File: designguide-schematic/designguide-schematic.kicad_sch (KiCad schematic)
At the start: 47 parts, among them J1 HRO_TYPE-C-31-M-14, J2 UDB, J3 Battery, J4 Battery, J5 Thermistor, Q1 AO3401A, Q2 2N7002, SW1 PWR, U1 SRV05-4, U2 TP4056, U3 BQ24075

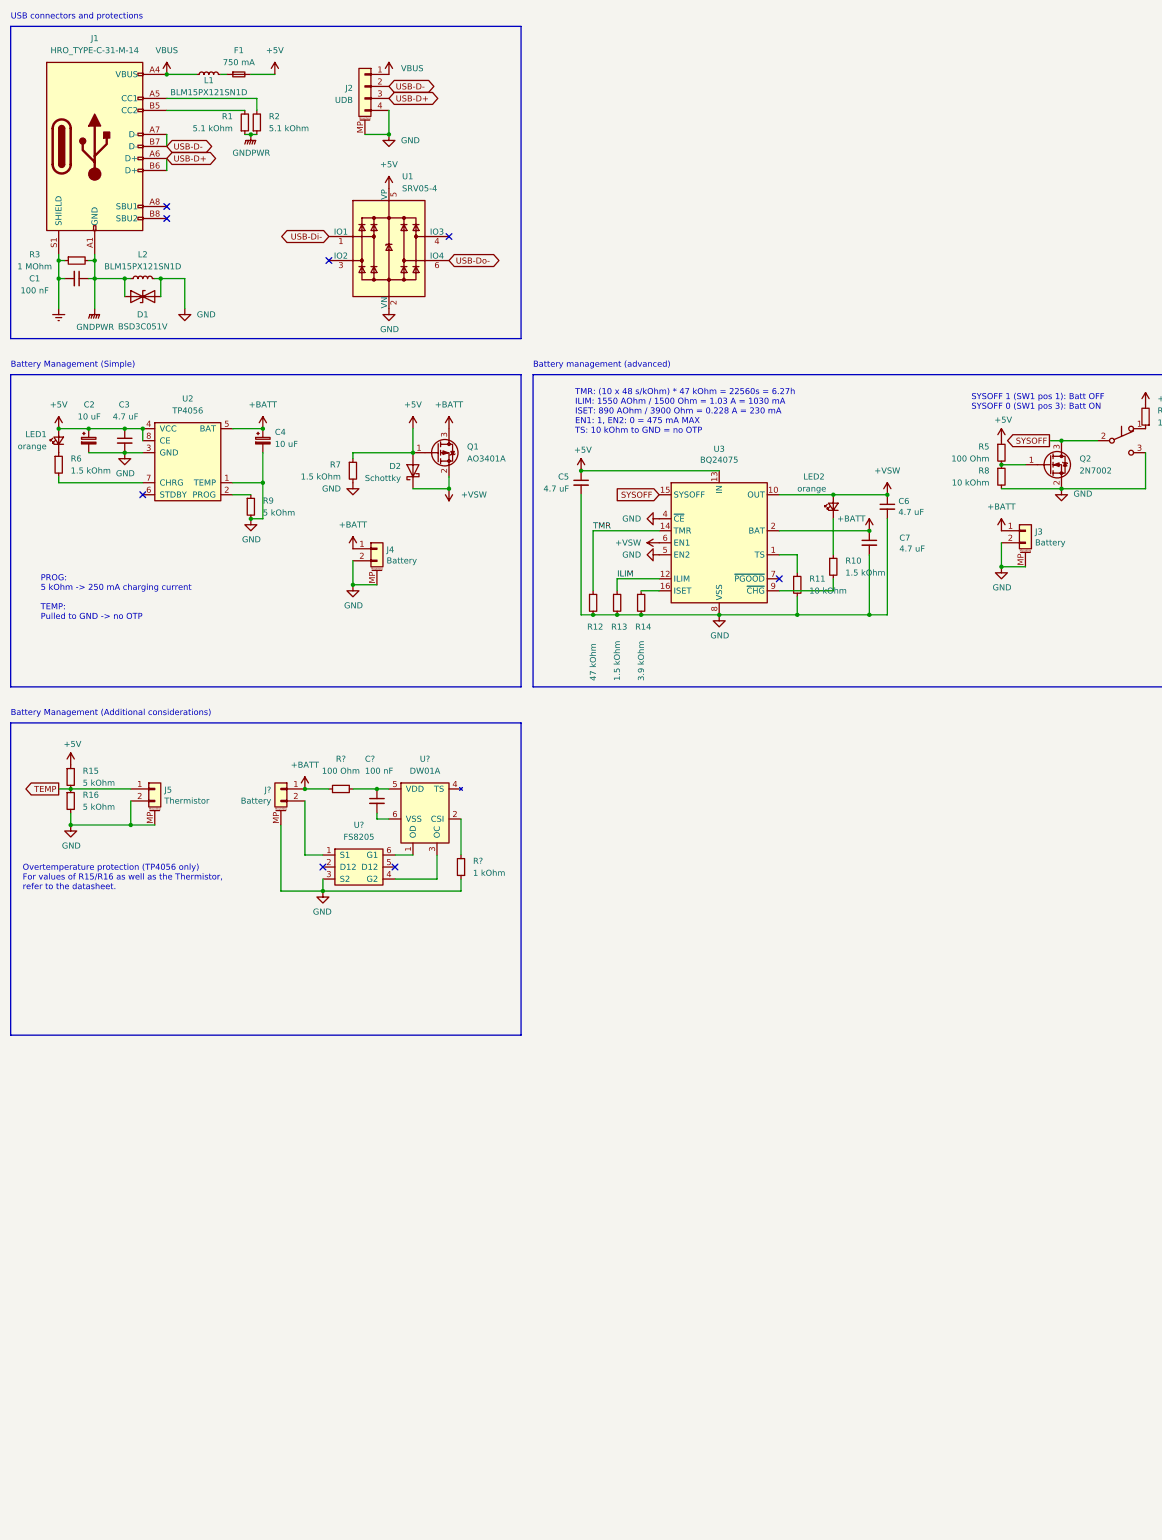
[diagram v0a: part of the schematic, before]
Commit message: readied battery management, usb, mcu parts
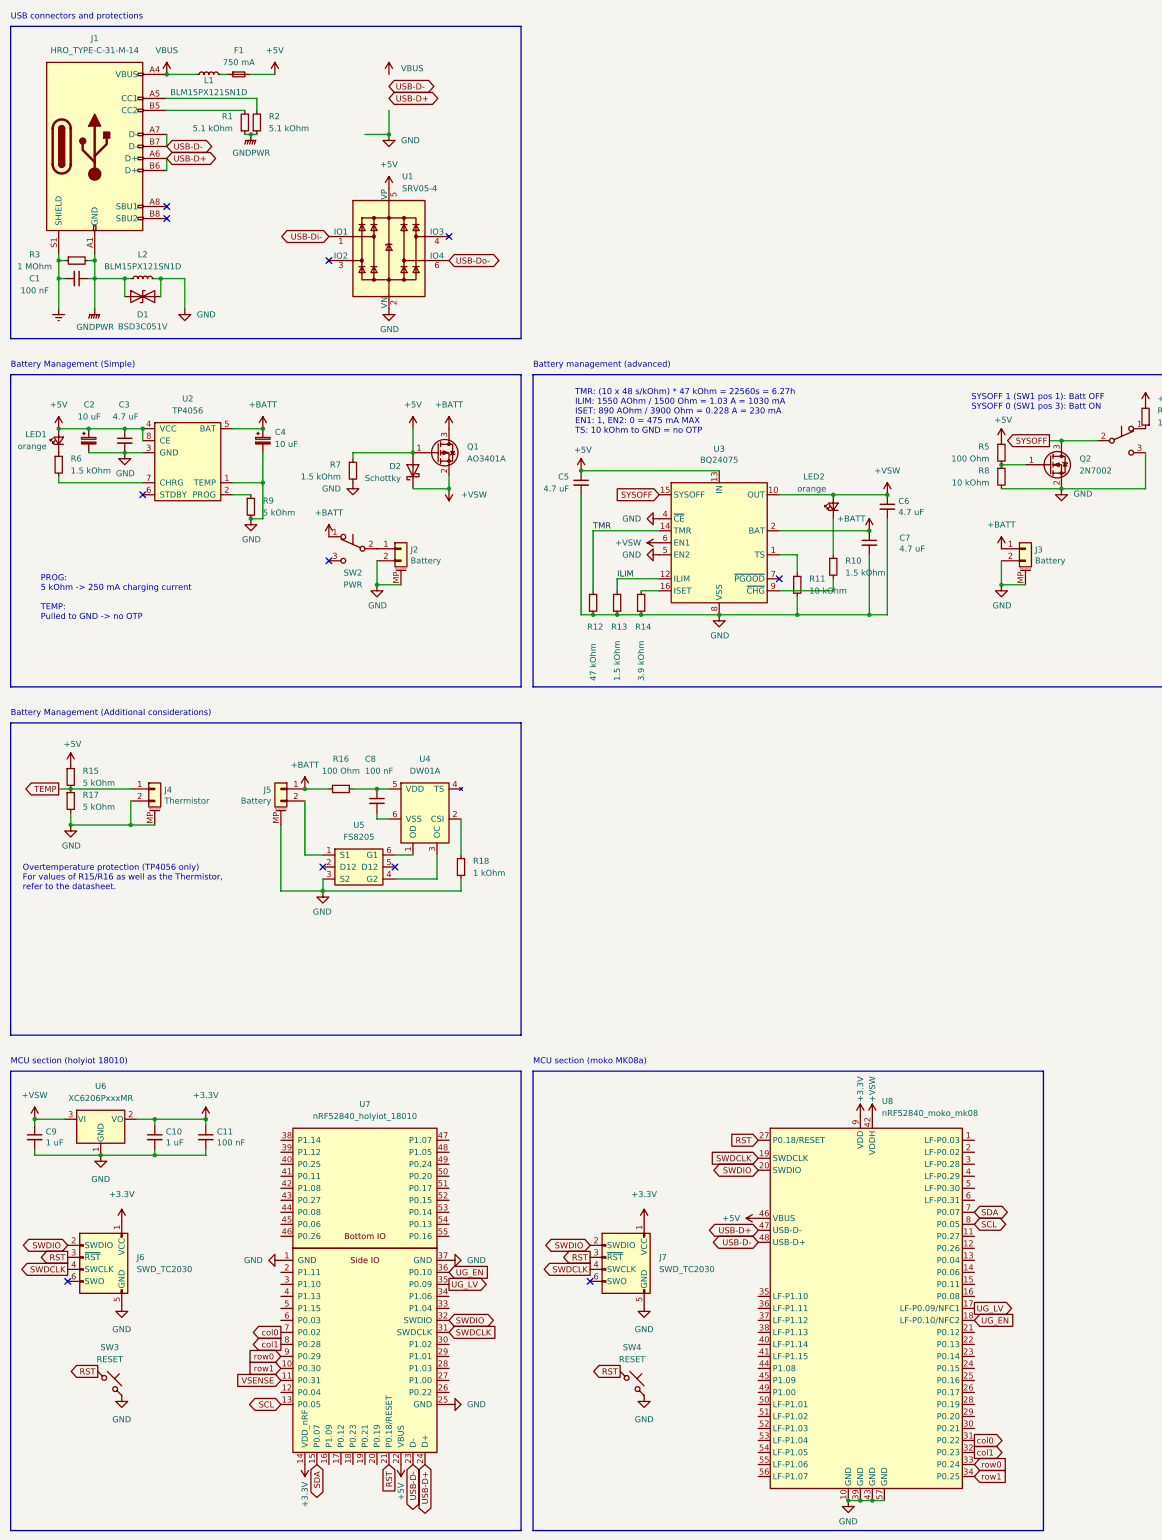
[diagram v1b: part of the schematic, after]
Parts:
- removed J2: UDB, Connector_JST:JST_SH_SM02B-SRSS-TB_1x02-1MP_P1.00mm_Horizontal, symbol Connector_Generic_MountingPin:Conn_01x04_MountingPin
- added C10, C9: 1 uF, Capacitor_SMD:C_0402_1005Metric, symbol Device:C_Small
- added C11: 100 nF, Capacitor_SMD:C_0402_1005Metric, symbol Device:C_Small
- added J6, J7: SWD_TC2030, marbastlib-various:CON_TC2030_outlined, symbol marbastlib-various:JTAG_TC2030
- added SW2: PWR, marbastlib-various:SW_MSK12C02-HB, symbol Switch:SW_Push_SPDT
- added SW3, SW4: RESET, symbol Switch:SW_Push_45deg
- added U6: XC6206PxxxMR, Package_TO_SOT_SMD:SOT-23, symbol Regulator_Linear:XC6206PxxxMR
- added U7: nRF52840_holyiot_18010, marbastlib-various:nRF52840_holyiot_18010, symbol marbastlib-various:nRF52840_holyiot_18010
- added U8: nRF52840_moko_mk08, marbastlib-various:nRF52840_moko_mk08, symbol marbastlib-various:nRF52840_moko_mk08
- gave numbers to parts that had none: 6
- renumbered J4 to J2, J5 to J4, R16 to R17
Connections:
- net +5V: now also U7.22 (VBUS), U8.46 (VBUS)
- net +BATT: now also SW2.1 (A); no longer J2.1 (Pin_1)
- net +VSW: now also C9.1, U6.3 (VI), U8.42 (VDDH)
- net GND: now also C10.2, C11.2, C9.2, J6.5 (GND), J7.5 (GND), SW3.2, SW4.2, U6.1 (GND), U7.1 (GND), U7.25 (GND), U7.37 (GND), U8.10 (GND), U8.39 (GND), U8.43 (GND), U8.57 (GND)
- net USB-D+: now also U7.24 (D+), U8.47 (USB-D-)
- net USB-D-: now also U7.23 (D-), U8.48 (USB-D+)
- new net: J2.1 (Pin_1), SW2.2 (B)
- new net +3.3V: C10.1, C11.1, J6.1 (VCC), J7.1 (VCC), U6.2 (VO), U7.14 (VDD_nRF), U8.9 (VDD)
- new net RST: J6.3 (~{RST}), J7.3 (~{RST}), SW3.1, SW4.1, U7.21 (P0.18/RESET), U8.27 (P0.18/RESET)
- new net SCL: U7.13 (P0.05), U8.8 (P0.05)
- new net SDA: U7.15 (P0.07), U8.7 (P0.07)
- new net SWDCLK: J6.4 (SWCLK), J7.4 (SWCLK), U7.31 (SWDCLK), U8.19 (SWDCLK)
- new net SWDIO: J6.2 (SWDIO), J7.2 (SWDIO), U7.32 (SWDIO), U8.20 (SWDIO)
- new net UG_EN: U7.36 (P0.10), U8.18 (LF-P0.10/NFC2)
- new net UG_LV: U7.35 (P0.09), U8.17 (LF-P0.09/NFC1)
- new net VSENSE: U7.11 (P0.31)
- new net col0: U7.7 (P0.02), U8.31 (P0.22)
- new net col1: U7.8 (P0.28), U8.32 (P0.23)
- new net row0: U7.9 (P0.29), U8.33 (P0.24)
- new net row1: U7.10 (P0.30), U8.34 (P0.25)
- no-connect marks 8 -> 11
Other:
- note added: "MCU section (holyiot 18010)"
- note added: "MCU section (moko MK08a)"
- moved on the sheet: J2, J3

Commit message: re-made images, finished schematic
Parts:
- added C12, C13, C14, C15, C16, C17, C18, C19: 100 nF, Capacitor_SMD:C_0402_1005Metric, symbol Device:C_Small
- added D3, D4, D5, D6: 1N4148WT, Diode_SMD:D_SOD-523, symbol Diode:1N4148WT
- added J2: UDB, symbol Connector_Generic_MountingPin:Conn_01x04_MountingPin
- added LED3, LED4, LED5, LED6, LED7, LED8, LED9: WS2812_2020, marbastlib-various:LED_WS2812_2020, symbol marbastlib-various:WS2812_2020
- added Q3: AO3401A, Package_TO_SOT_SMD:SOT-23, symbol Transistor_FET:AO3401A
- added Q4: 2N7002, Package_TO_SOT_SMD:SOT-23, symbol Transistor_FET:2N7002
- added R19, R20: 5.1 kOhm, Resistor_SMD:R_0402_1005Metric, symbol Device:R_Small
- added R21: 806 kOhm, Resistor_SMD:R_0402_1005Metric, symbol Device:R_Small
- added R22: 2 MOhm, Resistor_SMD:R_0402_1005Metric, symbol Device:R_Small
- added R23, R24, R26: 10 kOhm, Resistor_SMD:R_0402_1005Metric, symbol Device:R_Small
- added R25: 100 Ohm, Resistor_SMD:R_0402_1005Metric, symbol Device:R_Small
- added SW5, SW6, SW7, SW8: Keyswitch, symbol Switch:SW_Push_45deg
- added U10: TXB0101, Package_TO_SOT_SMD:SOT-363_SC-70-6_Handsoldering, symbol marbastlib-various:TXB0101
- added U9: MAX17048, Package_DFN_QFN:DFN-8-1EP_2x2mm_P0.5mm_EP0.7x1.3mm, symbol marbastlib-various:MAX17048
- renumbered J2 to J3, J3 to J4, J4 to J5, J5 to J6, J6 to J7, J7 to J8
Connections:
- net +3.3V: now also R19.2, R20.2, R23.1, U10.1 (VCCA)
- net +BATT: now also C12.2, U9.2 (CELL), U9.3 (VDD)
- net +VSW: now also Q3.3 (D), R21.1, R24.1, U10.6 (VCCB)
- net GND: now also C12.1, C13.1, C14.1, C15.1, C16.1, C17.1, C18.1, C19.1, J2.4 (Pin_4), J2.MP (MountPin), LED3.2 (VSS), LED4.2 (VSS), LED5.2 (VSS), LED6.2 (VSS), LED7.2 (VSS), LED8.2 (VSS), LED9.2 (VSS), Q4.2 (S), R22.2, R26.2, U10.2 (GND), U9.1 (CTG), U9.4 (GND), U9.6 (QSTRT), U9.9 (GND)
- net SCL: now also R19.1, U9.7 (SCL)
- net SDA: now also R20.1, U9.8 (SDA)
- net UG_EN: now also R25.1
- net UG_LV: now also U10.3 (A)
- net USB-D+: now also J2.3 (Pin_3)
- net USB-D-: now also J2.2 (Pin_2)
- net VBUS: now also J2.1 (Pin_1)
- net VSENSE: now also R21.2, R22.1
- net col0: now also SW5.1, SW7.1
- net col1: now also SW6.1, SW8.1
- net row0: now also D3.1 (K), D4.1 (K)
- net row1: now also D5.1 (K), D6.1 (K)
- new net: LED4.1 (DOUT), LED5.3 (DIN)
- new net: LED3.1 (DOUT), LED4.3 (DIN)
- new net: LED7.1 (DOUT), LED8.3 (DIN)
- new net: LED6.1 (DOUT), LED7.3 (DIN)
- new net: Q4.1 (G), R25.2, R26.1
- new net: Q3.1 (G), Q4.3 (D), R24.2
- new net: D3.2 (A), SW5.2
- new net: D5.2 (A), SW7.2
- new net: LED8.1 (DOUT), LED9.3 (DIN)
- new net: D6.2 (A), SW8.2
- new net: LED5.1 (DOUT), LED6.3 (DIN)
- new net: R23.2, U10.5 (OE)
- new net: D4.2 (A), SW6.2
- new net ALERT: U9.5 (~{ALRT})
- new net UG_HS: LED3.3 (DIN), U10.4 (B)
- new net UG_PWR: C13.2, C14.2, C15.2, C16.2, C17.2, C18.2, C19.2, LED3.4 (VDD), LED4.4 (VDD), LED5.4 (VDD), LED6.4 (VDD), LED7.4 (VDD), LED8.4 (VDD), LED9.4 (VDD), Q3.2 (S)
- no-connect marks 11 -> 12
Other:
- note added: "Switch matrix"
- note added: "Underglow enable"
- note added: "Underglow levelshifter"
- note added: "Voltage sensing (advanced)"
- note added: "Voltage sensing (simple) - Holyiot only!"

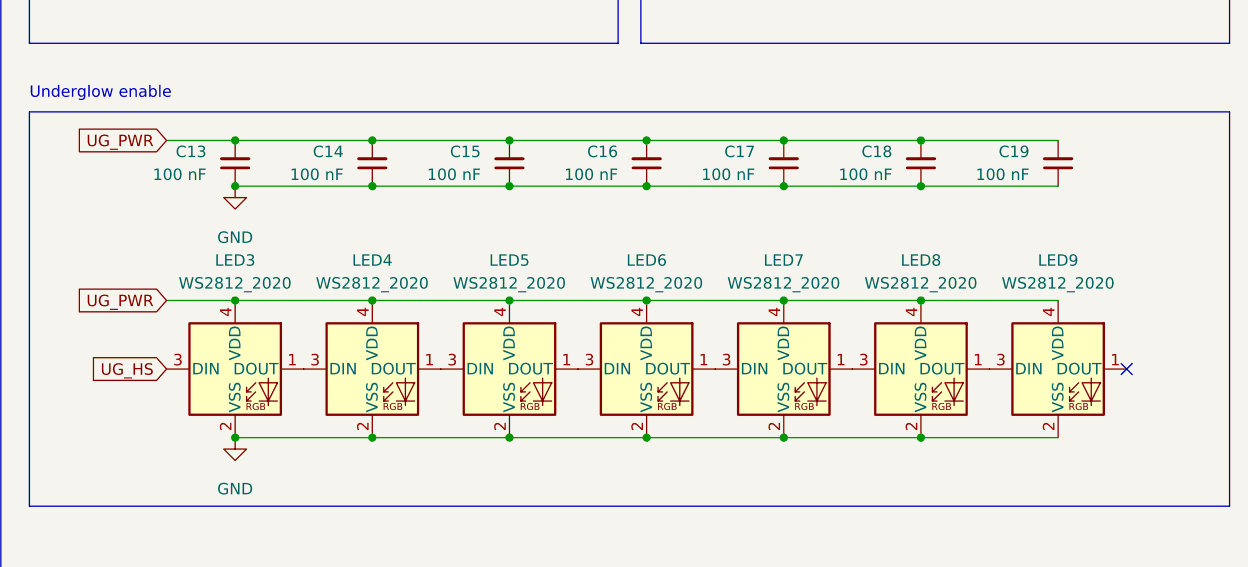
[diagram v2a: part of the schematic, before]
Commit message: included all pictures in the doc, changed underglow led model
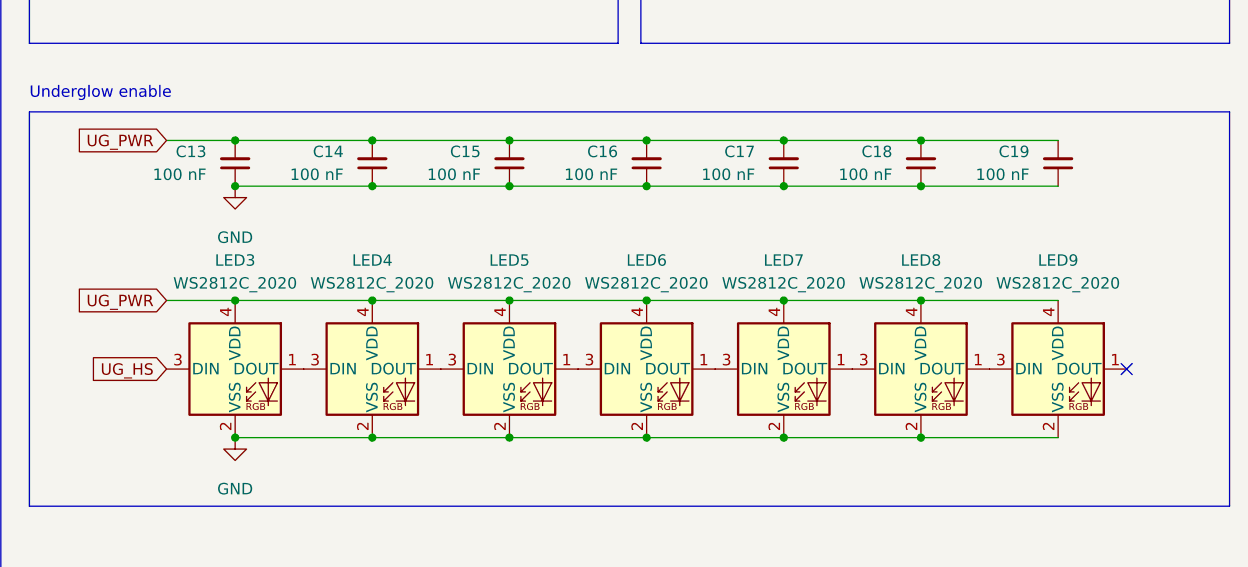
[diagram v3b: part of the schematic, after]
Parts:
- LED3, LED4, LED5, LED6, LED7, LED8, LED9: value WS2812_2020 -> WS2812C_2020
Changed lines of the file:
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@@
     (in_bom yes) (on_board yes)
     (property "Reference" "LED4" (id 0) (at 320.04 188.595 0))
-    (property "Value" "WS2812_2020" (id 1) (at 320.04 191.135 0))
+    (property "Value" "WS2812C_2020" (id 1) (at 320.04 191.135 0))
     (property "Footprint" "marbastlib-various:LED_WS2812_2020" (id 2) (at 321.31 208.28 0)
       (effects (font (size 1.27 1.27)) (justify left top) hide)
@@
     (in_bom yes) (on_board yes)
     (property "Reference" "LED7" (id 0) (at 365.76 188.595 0))
-    (property "Value" "WS2812_2020" (id 1) (at 365.76 191.135 0))
+    (property "Value" "WS2812C_2020" (id 1) (at 365.76 191.135 0))
     (property "Footprint" "marbastlib-various:LED_WS2812_2020" (id 2) (at 367.03 208.28 0)
       (effects (font (size 1.27 1.27)) (justify left top) hide)
@@
     (in_bom yes) (on_board yes)
     (property "Reference" "LED9" (id 0) (at 396.24 188.595 0))
-    (property "Value" "WS2812_2020" (id 1) (at 396.24 191.135 0))
+    (property "Value" "WS2812C_2020" (id 1) (at 396.24 191.135 0))
     (property "Footprint" "marbastlib-various:LED_WS2812_2020" (id 2) (at 397.51 208.28 0)
       (effects (font (size 1.27 1.27)) (justify left top) hide)
@@
     (in_bom yes) (on_board yes)
     (property "Reference" "LED6" (id 0) (at 350.52 188.595 0))
-    (property "Value" "WS2812_2020" (id 1) (at 350.52 191.135 0))
+    (property "Value" "WS2812C_2020" (id 1) (at 350.52 191.135 0))
     (property "Footprint" "marbastlib-various:LED_WS2812_2020" (id 2) (at 351.79 208.28 0)
       (effects (font (size 1.27 1.27)) (justify left top) hide)
@@
     (in_bom yes) (on_board yes)
     (property "Reference" "LED5" (id 0) (at 335.28 188.595 0))
-    (property "Value" "WS2812_2020" (id 1) (at 335.28 191.135 0))
+    (property "Value" "WS2812C_2020" (id 1) (at 335.28 191.135 0))
     (property "Footprint" "marbastlib-various:LED_WS2812_2020" (id 2) (at 336.55 208.28 0)
       (effects (font (size 1.27 1.27)) (justify left top) hide)
@@
     (in_bom yes) (on_board yes)
     (property "Reference" "LED3" (id 0) (at 304.8 188.595 0))
-    (property "Value" "WS2812_2020" (id 1) (at 304.8 191.135 0))
+    (property "Value" "WS2812C_2020" (id 1) (at 304.8 191.135 0))
     (property "Footprint" "marbastlib-various:LED_WS2812_2020" (id 2) (at 306.07 208.28 0)
       (effects (font (size 1.27 1.27)) (justify left top) hide)
@@
     (in_bom yes) (on_board yes)
     (property "Reference" "LED8" (id 0) (at 381 188.595 0))
-    (property "Value" "WS2812_2020" (id 1) (at 381 191.135 0))
+    (property "Value" "WS2812C_2020" (id 1) (at 381 191.135 0))
     (property "Footprint" "marbastlib-various:LED_WS2812_2020" (id 2) (at 382.27 208.28 0)
       (effects (font (size 1.27 1.27)) (justify left top) hide)
@@
     )
     (path "/be099aaf-91e7-4f30-bcfe-a826db791867"
-      (reference "LED3") (unit 1) (value "WS2812_2020") (footprint "marbastlib-various:LED_WS2812_2020")
+      (reference "LED3") (unit 1) (value "WS2812C_2020") (footprint "marbastlib-various:LED_WS2812_2020")
     )
     (path "/01e47efc-7fa8-4f1e-b6bf-44821f92b72f"
-      (reference "LED4") (unit 1) (value "WS2812_2020") (footprint "marbastlib-various:LED_WS2812_2020")
+      (reference "LED4") (unit 1) (value "WS2812C_2020") (footprint "marbastlib-various:LED_WS2812_2020")
     )
     (path "/98aa1401-b587-4e80-bbc7-8f0d7b960ad1"
-      (reference "LED5") (unit 1) (value "WS2812_2020") (footprint "marbastlib-various:LED_WS2812_2020")
+      (reference "LED5") (unit 1) (value "WS2812C_2020") (footprint "marbastlib-various:LED_WS2812_2020")
     )
     (path "/7f7491a6-ff42-4429-b106-a1814c6a1bac"
-      (reference "LED6") (unit 1) (value "WS2812_2020") (footprint "marbastlib-various:LED_WS2812_2020")
+      (reference "LED6") (unit 1) (value "WS2812C_2020") (footprint "marbastlib-various:LED_WS2812_2020")
     )
     (path "/0dc051c7-e2ee-424f-b9f6-bdc83c4e7eeb"
-      (reference "LED7") (unit 1) (value "WS2812_2020") (footprint "marbastlib-various:LED_WS2812_2020")
+      (reference "LED7") (unit 1) (value "WS2812C_2020") (footprint "marbastlib-various:LED_WS2812_2020")
     )
     (path "/dd1d51e2-eba3-4a1b-bb35-3fcf5b41b0da"
-      (reference "LED8") (unit 1) (value "WS2812_2020") (footprint "marbastlib-various:LED_WS2812_2020")
+      (reference "LED8") (unit 1) (value "WS2812C_2020") (footprint "marbastlib-various:LED_WS2812_2020")
     )
     (path "/43ecab9f-7b5e-4da2-9588-f5215e585b2f"
-      (reference "LED9") (unit 1) (value "WS2812_2020") (footprint "marbastlib-various:LED_WS2812_2020")
+      (reference "LED9") (unit 1) (value "WS2812C_2020") (footprint "marbastlib-various:LED_WS2812_2020")
     )
     (path "/499c7e3a-76ee-4850-98d7-4c853d391cad"
